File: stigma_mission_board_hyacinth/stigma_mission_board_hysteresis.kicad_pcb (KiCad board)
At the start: 4 copper layers, 50 x 150 mm, 209 parts, among them J10 Conn_02x02_Top_Bottom, J11 Conn_02x02_Top_Bottom, J12 Conn_02x02_Top_Bottom, J13 Conn_02x02_Top_Bottom, J2 Conn_02x05_Top_Bottom_Mountin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, J5 Conn_02x04_Top_Bottom, J6 Conn_02x04_Top_Bottom, J7 SMA, J8 SMA, J9 JST-GH 4Pin, Q1 DMN2056U, Q2 DMN2056U, Q3 AOSP21321, Q4 DMN2056U, Q5 AOSP21321, Q6 DMN2056U, Q7 AOSP21321, Q8 DMN2056U, Q9 AOSP21321, U1 LAN8742A, U10 MCP2562-E-SN, U11 MCP2562-E-SN, U12 SN74HCS594, U13 INA181, U14 INA181, U15 INA181, U16 INA181, U2 INA181, U3 TPD4E1U06, U4 L7805, U5 L7805, U6 AZ1117H-ADJ, U7 AZ1117H-ADJ, U8 Ai-Thinker-Ra-01, U9 Ai-Thinker-Ra-01, Y1 25MHz

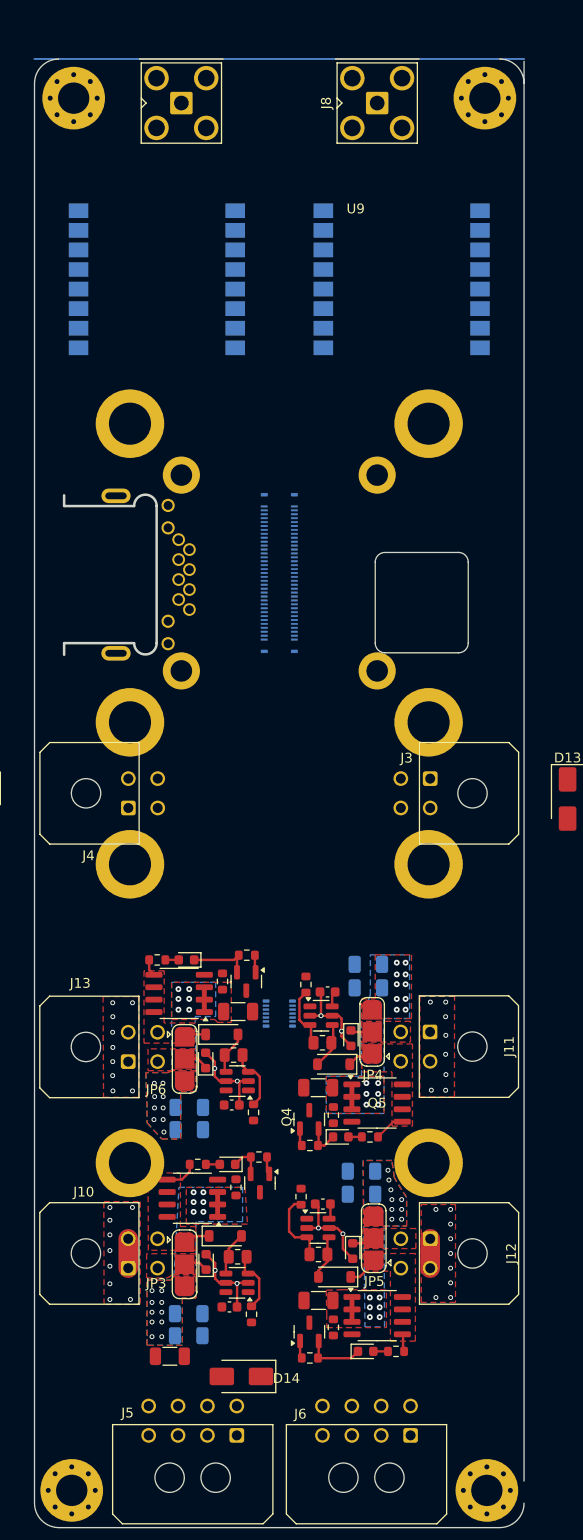
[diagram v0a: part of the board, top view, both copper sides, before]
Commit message: added 3d models of connectors
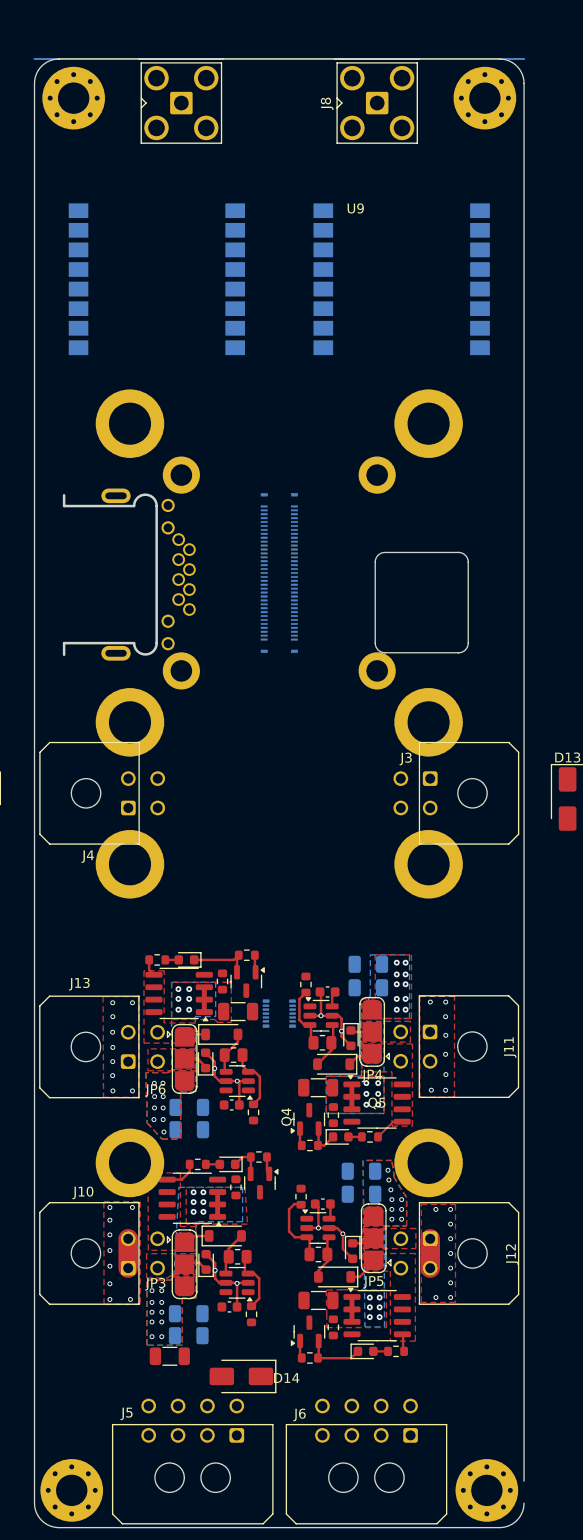
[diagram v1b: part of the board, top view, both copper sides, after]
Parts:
- J1: value ~ -> DF40C-70DS-0.4V(51)
- J10, J11, J12, J13: value Conn_02x02_Top_Bottom -> ~
- J2: value Conn_02x05_Top_Bottom_MountingPin -> DF40HB(2.5)-10DS-0.4V(51)
- J5, J6: value Conn_02x04_Top_Bottom -> ~
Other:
- outline, holes or cut-outs redrawn
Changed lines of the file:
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@@
 			)
 		)
-		(property "Description" "Generic connector, double row, 02x02, top/bottom pin numbering scheme (row 1: 1...pins_per_row, row2: pins_per_row+1 ... num_pins), script generated (kicad-library-utils/schlib/autogen/connector/)"
+		(property "Description" ""
 			(at 0 0 90)
 			(unlocked yes)
@@
 			)
 		)
-		(property "Value" "Conn_02x04_Top_Bottom"
+		(property "Value" "~"
 			(at 4.5 5.7 0)
 			(layer "F.Fab")
@@
 			)
 		)
-		(property "Description" "Generic connector, double row, 02x04, top/bottom pin numbering scheme (row 1: 1...pins_per_row, row2: pins_per_row+1 ... num_pins), script generated (kicad-library-utils/schlib/autogen/connector/)"
+		(property "Description" ""
 			(at 0 0 180)
 			(unlocked yes)
@@
 			)
 		)
-		(property "Value" "Conn_02x02_Top_Bottom"
+		(property "Value" "~"
 			(at 3.9 7.515 90)
 			(layer "F.Fab")
@@
 			)
 		)
-		(property "Description" "Generic connector, double row, 02x02, top/bottom pin numbering scheme (row 1: 1...pins_per_row, row2: pins_per_row+1 ... num_pins), script generated (kicad-library-utils/schlib/autogen/connector/)"
+		(property "Description" ""
 			(at 0 0 90)
 			(unlocked yes)
@@
 			)
 		)
-		(property "Description" "Generic connector, double row, 02x02, top/bottom pin numbering scheme (row 1: 1...pins_per_row, row2: pins_per_row+1 ... num_pins), script generated (kicad-library-utils/schlib/autogen/connector/)"
+		(property "Description" ""
 			(at 0 0 270)
 			(unlocked yes)
@@
 			)
 		)
-		(property "Value" "Conn_02x04_Top_Bottom"
+		(property "Value" "~"
 			(at 4.5 5.7 0)
 			(layer "F.Fab")
@@
 			)
 		)
-		(property "Description" "Generic connector, double row, 02x04, top/bottom pin numbering scheme (row 1: 1...pins_per_row, row2: pins_per_row+1 ... num_pins), script generated (kicad-library-utils/schlib/autogen/connector/)"
+		(property "Description" ""
 			(at 0 0 180)
 			(unlocked yes)
@@
 			)
 		)
-		(property "Value" "Conn_02x02_Top_Bottom"
+		(property "Value" "~"
 			(at 1.5 5.7 90)
 			(layer "F.Fab")
@@
 			)
 		)
-		(property "Description" "Generic connector, double row, 02x02, top/bottom pin numbering scheme (row 1: 1...pins_per_row, row2: pins_per_row+1 ... num_pins), script generated (kicad-library-utils/schlib/autogen/connector/)"
+		(property "Description" ""
 			(at 0 0 270)
 			(unlocked yes)
@@
 			)
 		)
-		(property "Value" "Conn_02x02_Top_Bottom"
+		(property "Value" "~"
 			(at 1.5 5.7 90)
 			(layer "F.Fab")
@@
 			)
 		)
-		(property "Description" "Generic connector, double row, 02x02, top/bottom pin numbering scheme (row 1: 1...pins_per_row, row2: pins_per_row+1 ... num_pins), script generated (kicad-library-utils/schlib/autogen/connector/)"
+		(property "Description" ""
 			(at 0 0 270)
 			(unlocked yes)
@@
 			)
 		)
-		(property "Value" "Conn_02x02_Top_Bottom"
+		(property "Value" "~"
 			(at 1.7 -10.02 90)
 			(layer "F.Fab")
@@
 			)
 		)
-		(property "Description" "Generic connector, double row, 02x02, top/bottom pin numbering scheme (row 1: 1...pins_per_row, row2: pins_per_row+1 ... num_pins), script generated (kicad-library-utils/schlib/autogen/connector/)"
+		(property "Description" ""
 			(at 0 0 90)
 			(unlocked yes)
@@
 			)
 		)
-		(property "Value" "Conn_02x05_Top_Bottom_MountingPin"
+		(property "Value" "DF40HB(2.5)-10DS-0.4V(51)"
 			(at 1.3 0 90)
 			(unlocked yes)
@@
 			)
 		)
-		(property "Datasheet" ""
+		(property "Datasheet" "https://www.hirose.com/en/product/document?clcode=&productname=&series=DF40&documenttype=Catalog&lang=en&documentid=en_DF40_CAT"
 			(at 3.7 0 90)
 			(unlocked yes)
@@
 			)
 		)
-		(property "Description" "Generic connectable mounting pin connector, double row, 02x05, top/bottom pin numbering scheme (row 1: 1...pins_per_row, row2: pins_per_row+1 ... num_pins), script generated (kicad-library-utils/schlib/autogen/connector/)"
+		(property "Description" "CONN RCPT 10POS SMD GOLD"
 			(at 3.7 0 90)
 			(unlocked yes)
@@
 			)
 		)
+		(property "LCSC#" "C5623558"
+			(at 0 0 270)
+			(unlocked yes)
+			(layer "B.Fab")
+			(hide yes)
+			(effects
+				(font
+					(size 1 1)
+					(thickness 0.15)
+				)
+				(justify mirror)
+			)
+		)
 		(property ki_fp_filters "Connector*:*_2x??-1MP*")
 		(sheetname "/")
@@
 		)
 		(embedded_fonts no)
+		(model "C:/Users/Marco/Documents/RAPID-Git/pcbs/stigma/common/3dmodels/df40hb_2_5_-10ds-0_4v_51_.stp"
+			(offset
+				(xyz -4.88 0 0.5)
+			)
+			(scale
+				(xyz 1 0.5 1)
+			)
+			(rotate
+				(xyz -90 -0 -90)
+			)
+		)
 	)
 	(footprint "Fuse:Fuse_1206_3216Metric"
@@
 			)
 		)
-		(property "Value" "~"
+		(property "Value" "DF40C-70DS-0.4V(51)"
 			(at 0 0 90)
 			(unlocked yes)
@@
 			)
 		)
-		(property "Datasheet" ""
+		(property "Datasheet" "https://www.hirose.com/en/product/document?clcode=&productname=&series=DF40&documenttype=Catalog&lang=en&documentid=en_DF40_CAT"
 			(at 0 0 90)
 			(unlocked yes)
@@
 			)
 		)
+		(property "LCSC#" "C294854"
+			(at 0 0 270)
+			(unlocked yes)
+			(layer "B.Fab")
+			(hide yes)
+			(effects
+				(font
+					(size 1 1)
+					(thickness 0.15)
+				)
+				(justify mirror)
+			)
+		)
 		(property ki_fp_filters "Connector*:*_2x??-1SH*")
 		(sheetname "/")
@@
 			(size 7 7)
 			(drill 4.3)
-			(layers "*.Cu" "*.Mask")
+			(layers "F&B.Cu" "*.Mask")
 			(remove_unused_layers no)
 		)
@@
 			(size 7 7)
 			(drill 4.3)
-			(layers "*.Cu" "*.Mask")
+			(layers "F&B.Cu" "*.Mask")
 			(remove_unused_layers no)
 		)
@@
 			(drill 2.2)
 			(property pad_prop_castellated)
-			(layers "*.Cu" "*.Mask")
+			(layers "F&B.Cu" "*.Mask")
 			(remove_unused_layers no)
 		)
@@
 			(size 3.8 3.8)
 			(drill 2.2)
-			(layers "*.Cu" "*.Mask")
+			(layers "F&B.Cu" "*.Mask")
 			(remove_unused_layers no)
 		)
@@
 			(size 3.8 3.8)
 			(drill 2.2)
-			(layers "*.Cu" "*.Mask")
+			(layers "F&B.Cu" "*.Mask")
 			(remove_unused_layers no)
 		)
@@
 			(size 3.8 3.8)
 			(drill 2.2)
-			(layers "*.Cu" "*.Mask")
+			(layers "F&B.Cu" "*.Mask")
 			(remove_unused_layers no)
 		)
@@
 			(size 7 7)
 			(drill 4.3)
-			(layers "*.Cu" "*.Mask")
+			(layers "F&B.Cu" "*.Mask")
 			(remove_unused_layers no)
 		)
@@
 			(size 7 7)
 			(drill 4.3)
-			(layers "*.Cu" "*.Mask")
+			(layers "F&B.Cu" "*.Mask")
 			(remove_unused_layers no)
 		)
@@
 		)
 		(embedded_fonts no)
+		(model "C:/Users/Marco/Documents/RAPID-Git/pcbs/stigma/common/3dmodels/df40c-70ds-0_4v_51_.stp"
+			(offset
+				(xyz -1.11 0 0)
+			)
+			(scale
+				(xyz 1 1 1)
+			)
+			(rotate
+				(xyz -90 -0 90)
+			)
+		)
 	)
 	(gr_line
@@
 	)
 	(gr_line
-		(start 250 100.24)
+		(start 250 102.5)
 		(end 250 245.24)
 		(stroke
@@
 		(stroke
 			(width 0.05)
+			(type default)
+		)
+		(layer "Edge.Cuts")
+	)
+	(gr_line
+		(start 247.5 100)
+		(end 202.5 100)
+		(stroke
+			(width 0.05)

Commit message: rearanged some stuff
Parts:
- moved D27 5.52 mm to (215.4, 186.5)
- moved R60 5.52 mm to (212.4, 186.5)
- moved J1 5.00 mm to (225.0, 157.5), turned to 180 degrees
- moved J3 5.00 mm to (240.4, 178.5)
- moved J4 5.00 mm to (209.6, 181.5)
- moved RJ1 5.00 mm to (212.1, 157.7)
- moved F1 3.00 mm to (215.8, 212.4)
- moved R52 2.42 mm to (232.1, 211.2), turned to 0 degrees
- moved J2 1.89 mm to (225.0, 199.4)
- moved C49 1.52 mm to (229.7, 218.4)
- moved D24 1.52 mm to (234.1, 233.5)
- moved J12 1.52 mm to (240.7, 222.0)
- moved Q6 1.52 mm to (228.3, 231.5)
- moved R55 1.52 mm to (227.5, 217.7)
- moved U15 1.52 mm to (229.2, 220.9)
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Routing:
- net GND: track 79.2 -> 74.4 mm
- net /Recovery Output2/recovery_switched: track 5.74 -> 3.54 mm
- net /Recovery Output 1/recovery_switched: track 3.87 -> 2.15 mm
- net Net-(D21-A): track 1.38 -> 0.00 mm
- net Net-(D27-A): track 1.37 -> 0.00 mm
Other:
- outline, holes or cut-outs redrawn
- board text added: "take a look"
- board text removed: "this one is not yet edited bc it's not yet clear whether we can remove the copper around the MP or not"

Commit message: changed pcb design. currently not working
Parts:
- removed the H2 at (89.0, 160.4)
- removed the H3 at (89.0, 168.3)
- removed H7, H8: MountingHole_Pad, MountingHole:MountingHole_3.2mm_M3_Pad_Via
- R41, U10: moved to B.Cu
- moved H5 149.5 mm to (246.5, 175.7)
- moved U10 145.7 mm to (242.5, 233.1), turned to -90 degrees
- moved R40 142.8 mm to (242.6, 233.7), turned to 0 degrees
- moved H2 114.5 mm to (203.5, 175.7)
- moved U11 113.5 mm to (207.6, 233.2), turned to -90 degrees
- moved R41 110.8 mm to (207.5, 233.6), turned to 180 degrees
- moved R43 79.9 mm to (235.3, 130.1)
- moved R44 75.6 mm to (232.3, 130.1)
- moved Q1 72.4 mm to (232.5, 127.4), turned to 90 degrees
- moved J9 71.5 mm to (239.5, 115.3)
- moved D16 67.0 mm to (233.0, 123.3)
- moved BZ1 66.4 mm to (239.2, 123.6)
- moved R31 31.1 mm to (108.7, 201.9)
- moved R30 24.9 mm to (108.4, 204.1)
- moved D12 21.4 mm to (107.6, 218.7), turned to 180 degrees
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- renumbered H4 to H2, H5 to H3, H6 to H4, H9 to H5, H10 to H6
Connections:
- R23 pad 1: high_current -> high_current_2
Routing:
- net GND: track 74.4 -> 88.9 mm, vias 67 -> 73
- net Net-(D10-A): track 0.00 -> 9.82 mm, vias 0 -> 2
- net Net-(D9-A): track 0.00 -> 9.81 mm, vias 0 -> 2
- net +5V: track 4.92 -> 11.8 mm, vias 0 -> 2
- net +3.3V: track 3.16 -> 8.41 mm
- net Net-(U6-GND): track 0.00 -> 4.05 mm, vias 0 -> 1
- net Net-(U7-GND): track 0.00 -> 3.61 mm, vias 0 -> 1
- net Net-(D11-A): track 0.00 -> 2.19 mm
- net Net-(D12-A): track 0.00 -> 2.15 mm
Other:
- board text added: "Das hier geht doch trotzdem nicht, oder?"
- board text added: "das hier könnte/müsste wieder {dblquote}symmetrisiert{dblquote} werden"
- board text removed: "Buzzer + DAC"
- board text removed: "CAN"
